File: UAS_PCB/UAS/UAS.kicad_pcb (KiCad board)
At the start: 2 copper layers, 50.8 x 47.6 mm, 17 parts, among them J1 SM02B-PASS-TBT, J2 SM02B-PASS-TBT, J3 SM02B-PASS-TBT, J4 SM02B-PASS-TBT, U1 JST-7-Pin, U10 UAS-rescue_7.5V-2.4A-Converte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, U11 JST-3-Pin, U12 Signal-Pad, U13 Signal-Pad, U2 5A-5V-Converter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

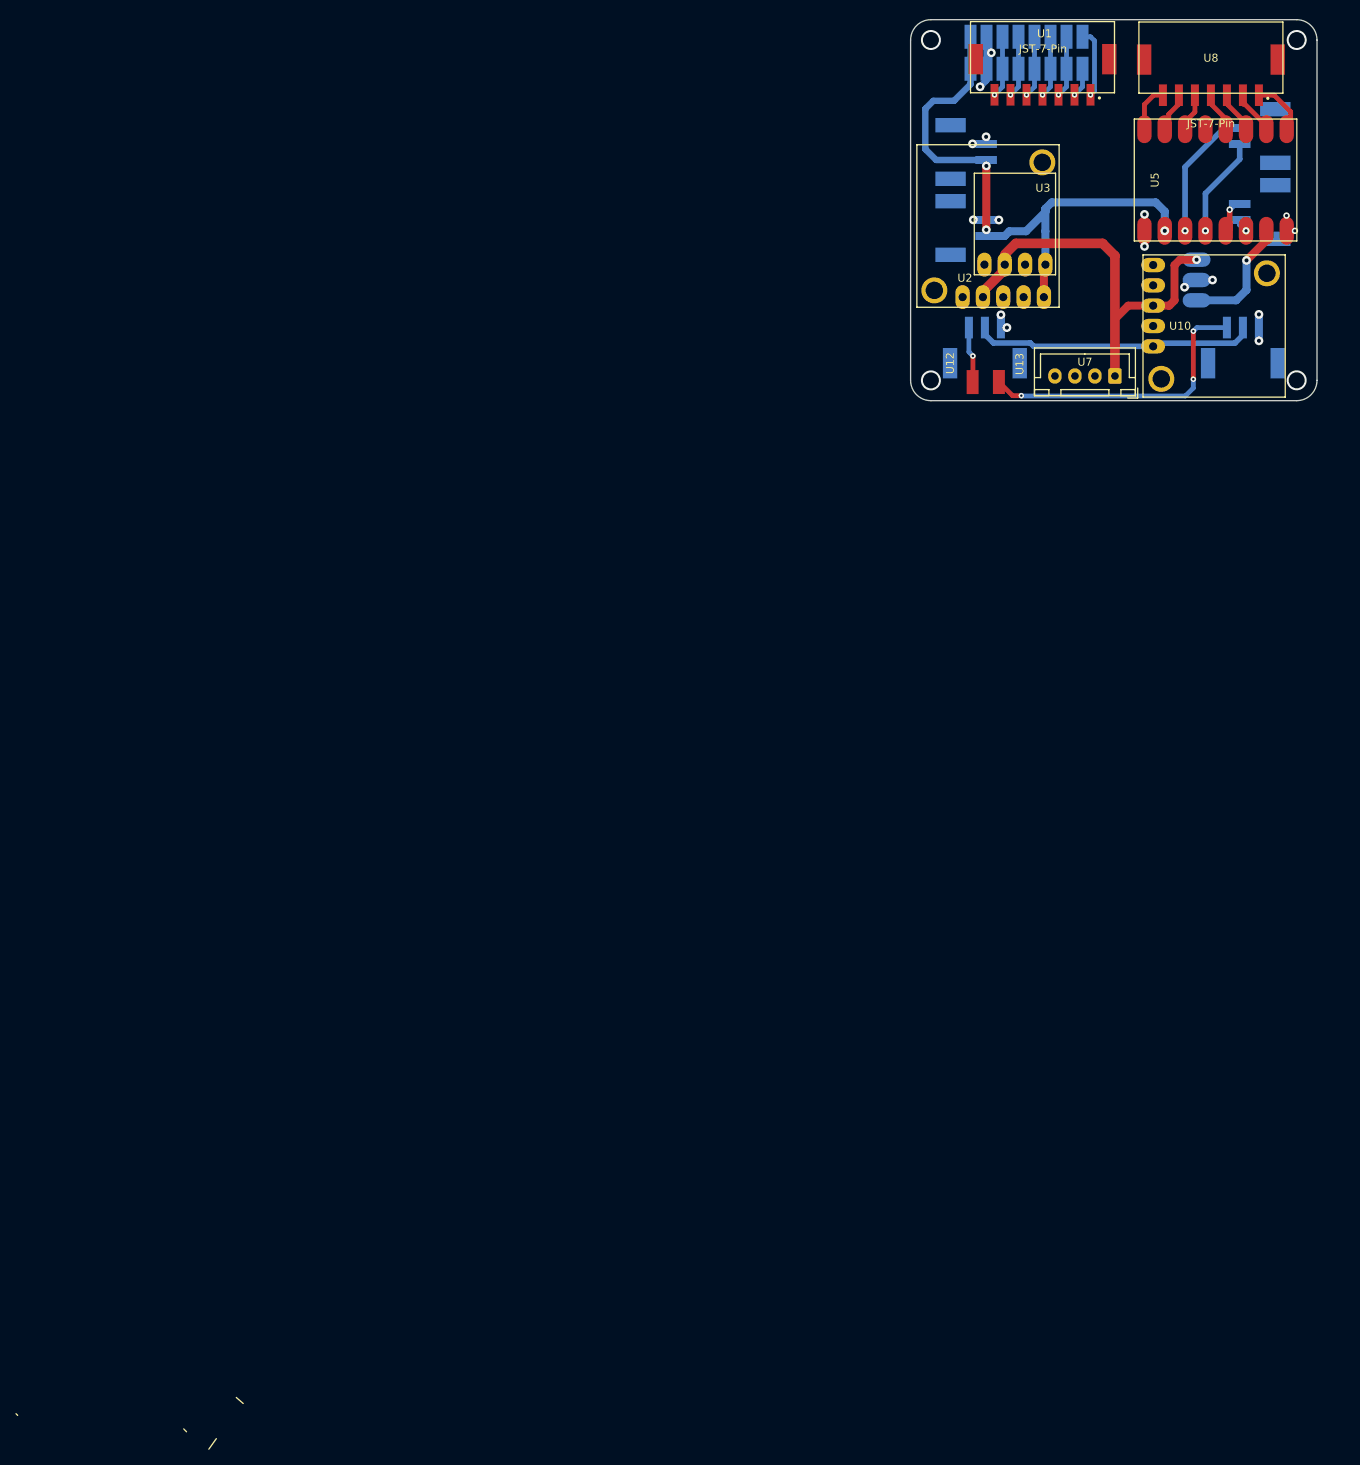
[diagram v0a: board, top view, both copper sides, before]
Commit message: Some vias and traces repositioned
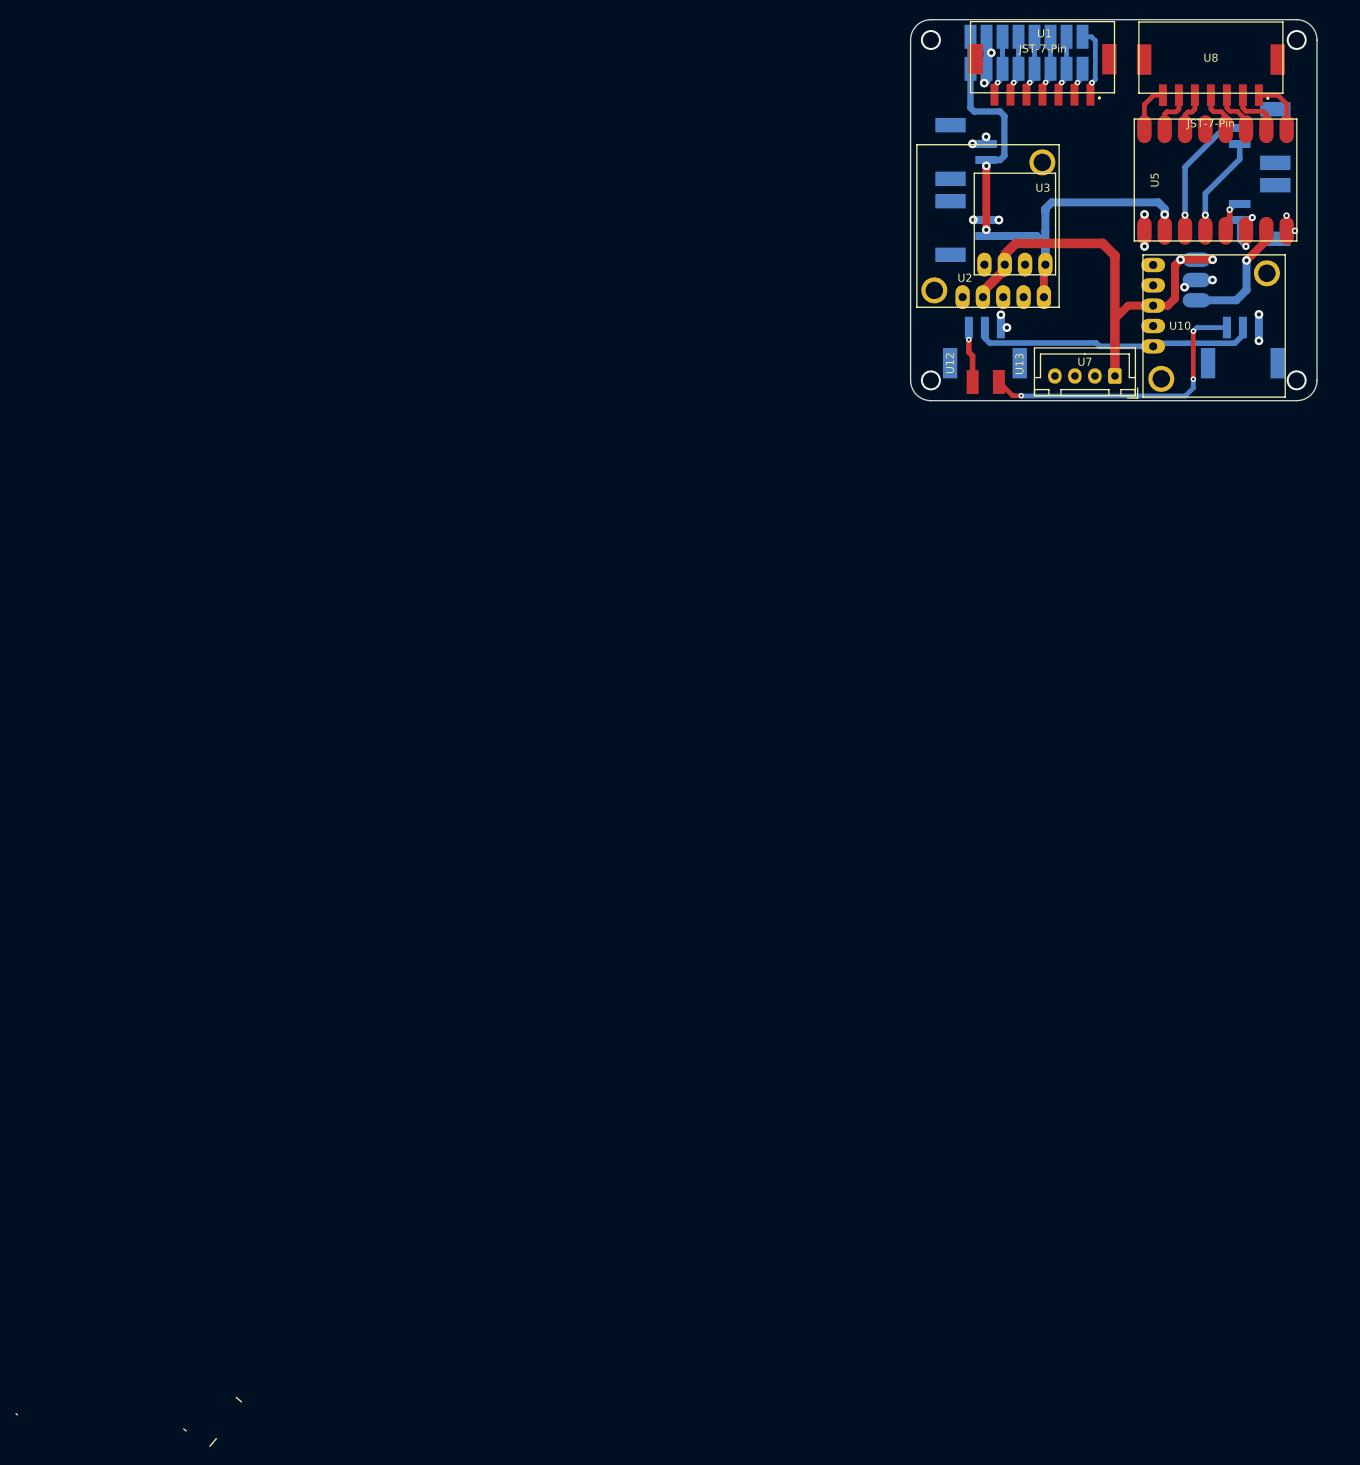
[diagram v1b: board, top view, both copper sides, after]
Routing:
- net Net-(J2-Pad2): track 1.68 -> 9.26 mm, vias 1 -> 2
- net GND: track 24.3 -> 31.8 mm
- net +12V: track 55.6 -> 61.4 mm, vias 1 -> 2
- net +5V: track 75.8 -> 71.9 mm
- net Net-(U5-Pad13): track 5.22 -> 6.37 mm
- net Net-(U5-Pad14): track 6.07 -> 7.15 mm
- net Net-(U5-Pad15): track 6.07 -> 7.02 mm
- net Net-(U5-Pad10): track 4.78 -> 5.66 mm
- net Net-(U5-Pad11): track 4.55 -> 5.06 mm

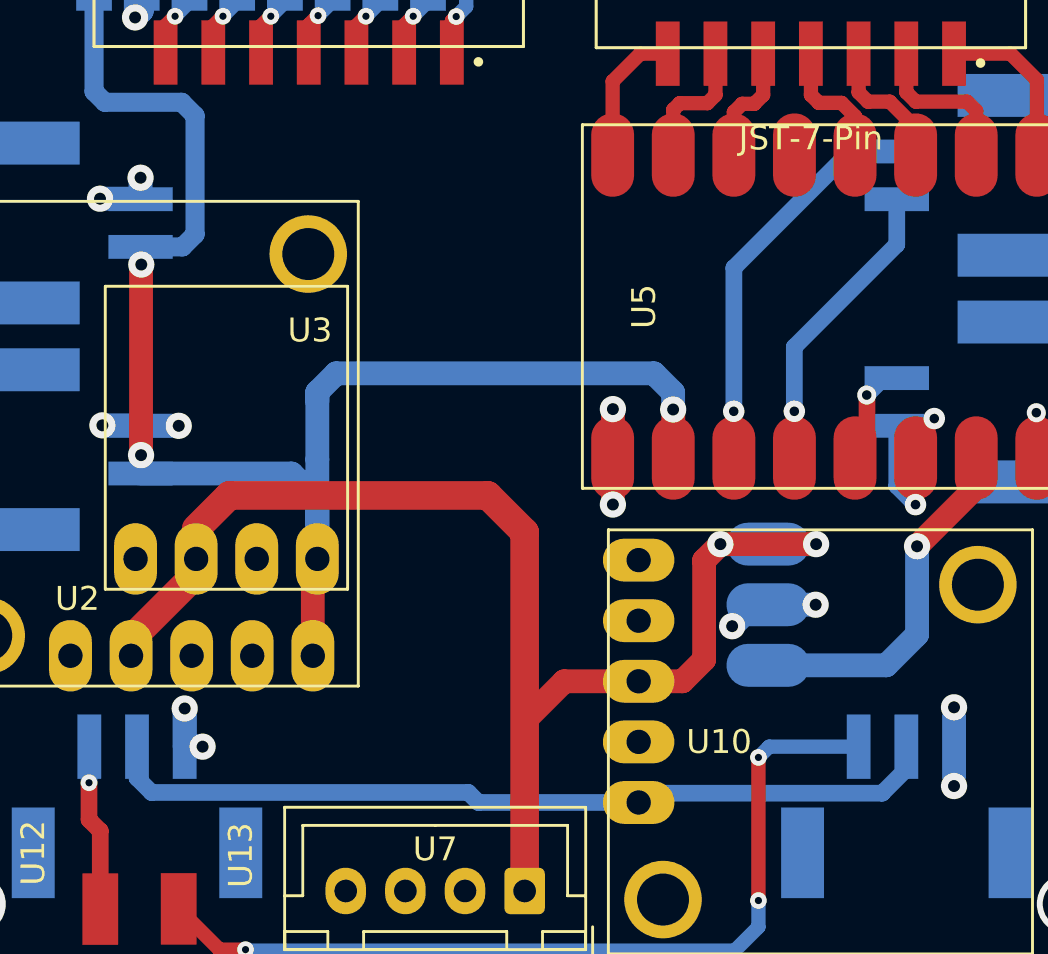
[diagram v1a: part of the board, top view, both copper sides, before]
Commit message: Pair of traces moved
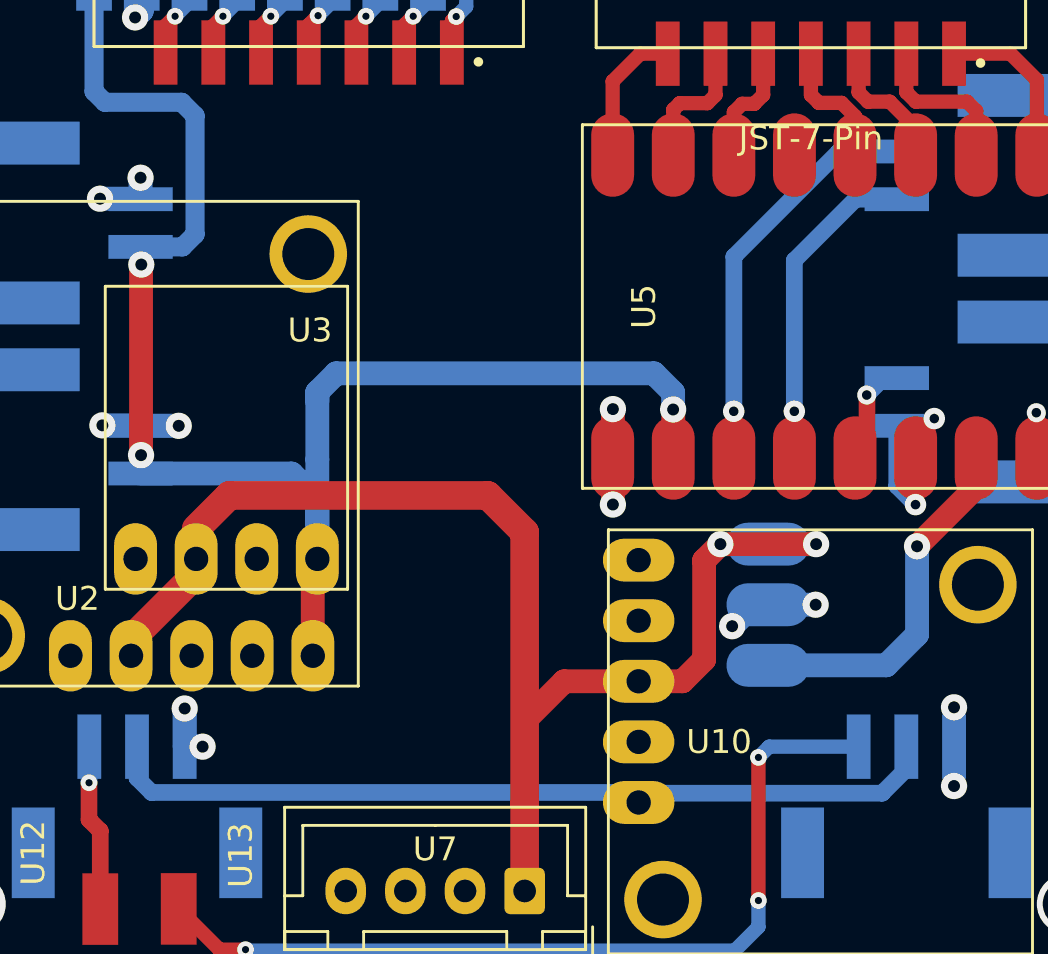
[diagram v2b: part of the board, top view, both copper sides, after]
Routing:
- net Net-(J1-Pad2): track 12.6 -> 13.6 mm

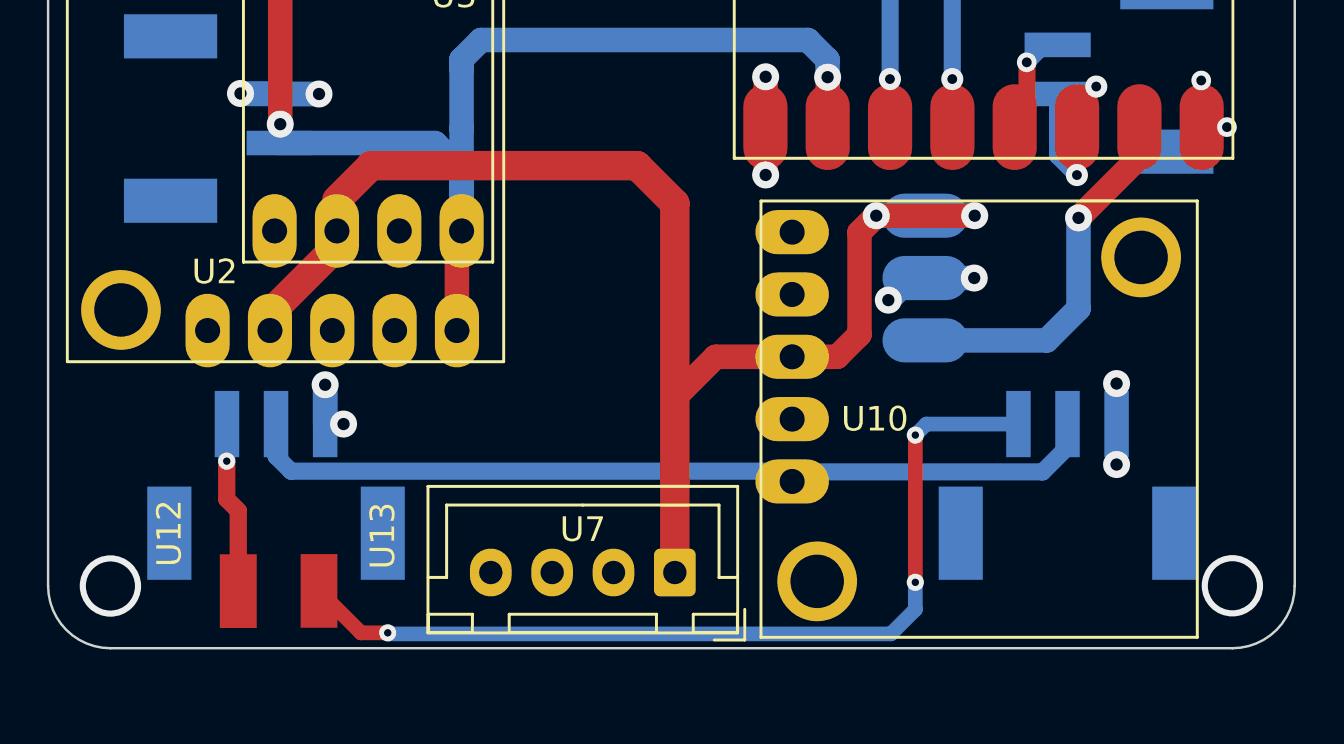
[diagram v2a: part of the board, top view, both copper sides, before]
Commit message: trace width changes
i blame rani, still need lbr payload logo
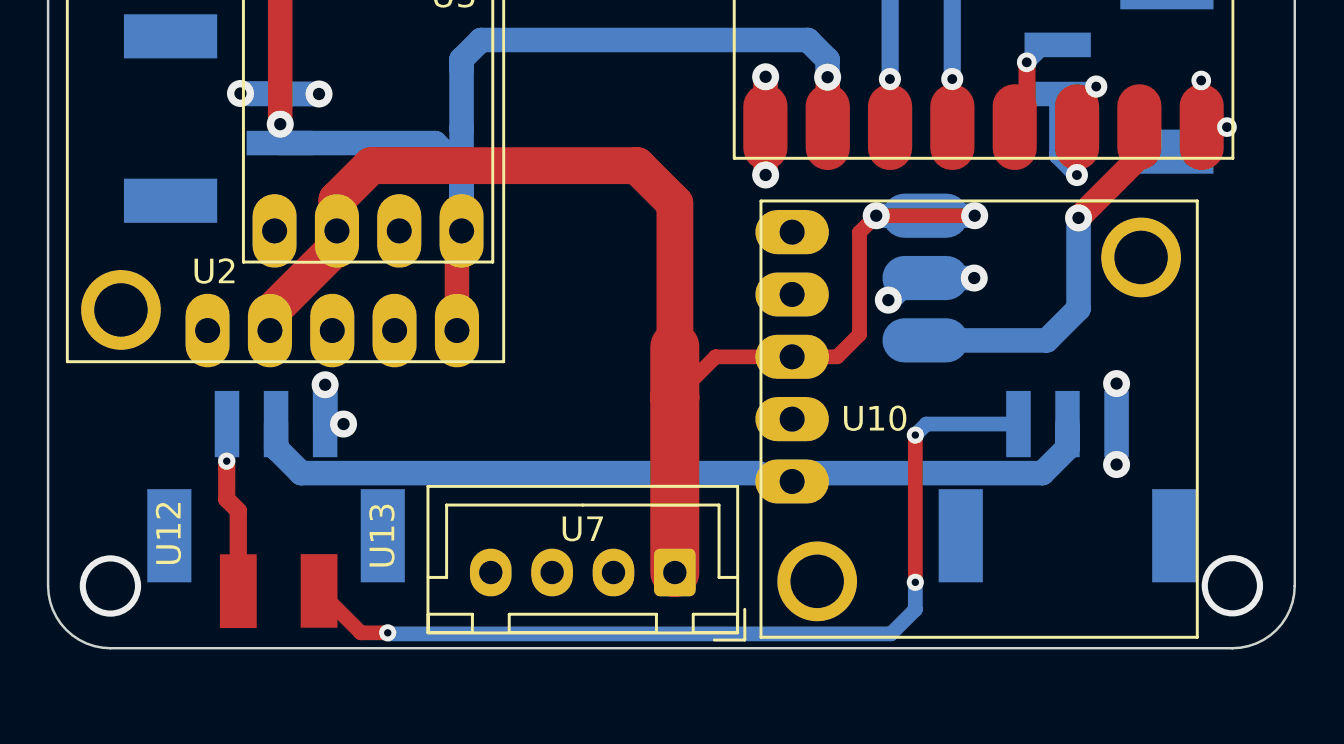
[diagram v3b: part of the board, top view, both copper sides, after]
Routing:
- net +7.5V: track 38.9 -> 35.2 mm
- net +12V: track 61.4 -> 58.2 mm
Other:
- board text added: "JLCJLCJLCJLCJLC"

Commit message: final version with kyles passthrough pads and graphics
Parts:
- added U14: UAS-rescue_Signal-Pad-UAS-cache, UAS:Individual_Solder_Pad, F.Cu at (137.2, 111.5)
- added U15: UAS-rescue_Signal-Pad-UAS-cache, UAS:Individual_Solder_Pad, F.Cu at (166.6, 107.8)
- added U16: UAS-rescue_Signal-Pad-UAS-cache, UAS:Individual_Solder_Pad, F.Cu at (140.8, 111.5)
- added U17: UAS-rescue_Signal-Pad-UAS-cache, UAS:Individual_Solder_Pad, F.Cu at (166.6, 111.1)
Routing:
- net Net-(U14-Pad1): track 0.00 -> 59.0 mm, vias 0 -> 4
- net Net-(U16-Pad1): track 0.00 -> 35.7 mm, vias 0 -> 2

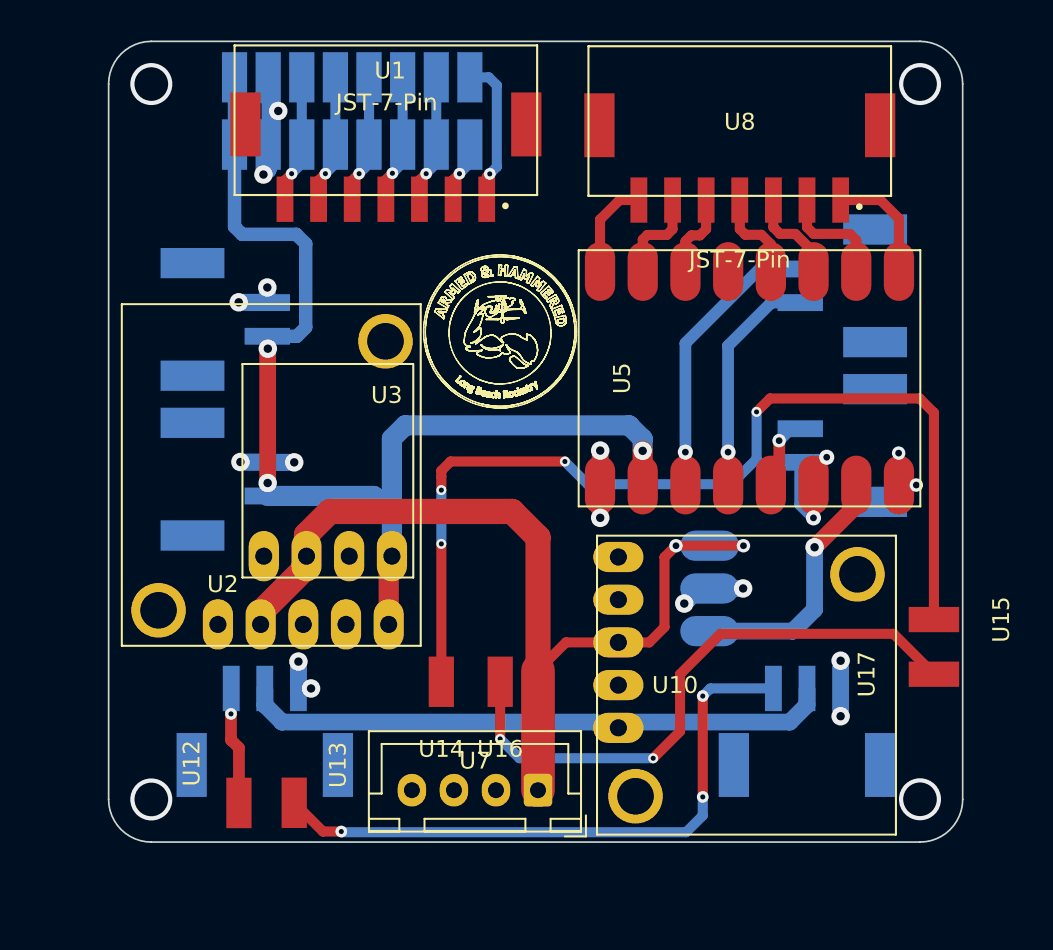
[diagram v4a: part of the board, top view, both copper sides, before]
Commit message: filled ground plane attempt 1
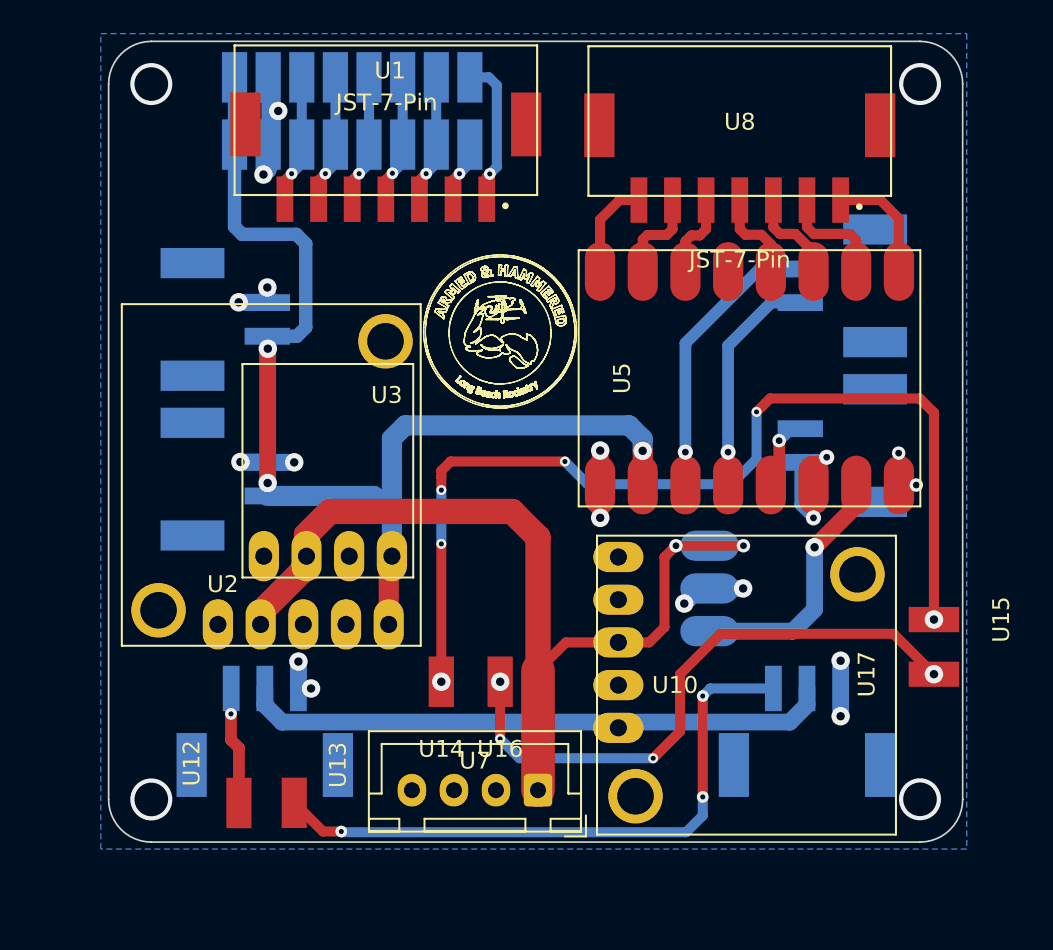
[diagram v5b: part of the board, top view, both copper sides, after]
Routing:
- net Net-(U16-Pad1): vias 2 -> 4
- net Net-(U14-Pad1): vias 4 -> 6
- added copper zone on B.Cu, net GND
